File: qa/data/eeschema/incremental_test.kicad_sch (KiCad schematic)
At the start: 2 parts

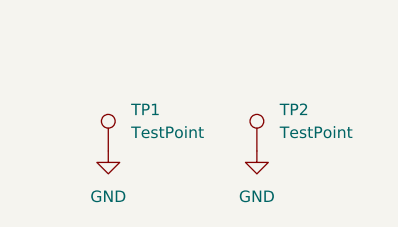
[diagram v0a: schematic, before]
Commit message: feat: update kicad to 9.0.0+dfsg-1
Signed-off-by: lhdjply <lhdjply@126.com>
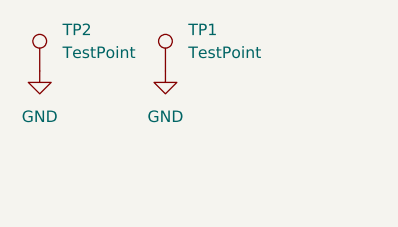
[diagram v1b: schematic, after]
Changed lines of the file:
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@@
 (kicad_sch
-	(version 20231120)
+	(version 20240101)
 	(generator "eeschema")
-	(generator_version "8.0")
+	(generator_version "8.99")
 	(paper "A4")
 	(symbol
+		(lib_id "power:GND")
+		(at 74.93 80.01 0)
+		(unit 1)
+		(exclude_from_sim no)
+		(in_bom yes)
+		(on_board yes)
+		(dnp no)
+		(fields_autoplaced yes)
+		(property "Reference" "#PWR03"
+			(at 74.93 86.36 0)
+			(effects
+				(font
+					(size 1.27 1.27)
+				)
+				(hide yes)
+			)
+		)
+		(property "Value" "GND"
+			(at 74.93 85.09 0)
+			(effects
+				(font
+					(size 1.27 1.27)
+				)
+			)
+		)
+		(property "Footprint" ""
+			(at 74.93 80.01 0)
+			(effects
+				(font
+					(size 1.27 1.27)
+				)
+				(hide yes)
+			)
+		)
+		(property "Datasheet" ""
+			(at 74.93 80.01 0)
+			(effects
+				(font
+					(size 1.27 1.27)
+				)
+				(hide yes)
+			)
+		)
+		(property "Description" "Power symbol creates a global label with name \"GND\" , ground"
+			(at 74.93 80.01 0)
+			(effects
+				(font
+					(size 1.27 1.27)
+				)
+				(hide yes)
+			)
+		)
+		(pin "1"
+		)
+		(instances
+			(project "incremental_test"
+				(path "/9c07925a-2c60-43f0-9bac-88be11f9747d"
+					(reference "#PWR03")
+					(unit 1)
+				)
+			)
+		)
+	)
+	(symbol
 		(lib_id "Connector:TestPoint")
-		(at 82.55 88.9 0)
+		(at 74.93 80.01 0)
+		(unit 1)
+		(exclude_from_sim no)
+		(in_bom yes)
+		(on_board yes)
+		(dnp no)
+		(fields_autoplaced yes)
+		(property "Reference" "TP2"
+			(at 77.47 75.4379 0)
+			(effects
+				(font
+					(size 1.27 1.27)
+				)
+				(justify left)
+			)
+		)
+		(property "Value" "TestPoint"
+			(at 77.47 77.9779 0)
+			(effects
+				(font
+					(size 1.27 1.27)
+				)
+				(justify left)
+			)
+		)
+		(property "Footprint" ""
+			(at 80.01 80.01 0)
+			(effects
+				(font
+					(size 1.27 1.27)
+				)
+				(hide yes)
+			)
+		)
+		(property "Datasheet" "~"
+			(at 80.01 80.01 0)
+			(effects
+				(font
+					(size 1.27 1.27)
+				)
+				(hide yes)
+			)
+		)
+		(property "Description" "test point"
+			(at 74.93 80.01 0)
+			(effects
+				(font
+					(size 1.27 1.27)
+				)
+				(hide yes)
+			)
+		)
+		(pin "1"
+		)
+		(instances
+			(project "incremental_test"
+				(path "/9c07925a-2c60-43f0-9bac-88be11f9747d"
+					(reference "TP2")
+					(unit 1)
+				)
+			)
+		)
+	)
+	(symbol
+		(lib_id "Connector:TestPoint")
+		(at 88.9 80.01 0)
 		(unit 1)
 		(exclude_from_sim no)
@@
 		(fields_autoplaced yes)
 		(property "Reference" "TP1"
-			(at 85.09 84.328 0)
+			(at 91.44 75.4379 0)
 			(effects
 				(font
@@
 		)
 		(property "Value" "TestPoint"
-			(at 85.09 86.868 0)
-			(effects
-				(font
-					(size 1.27 1.27)
-				)
-				(justify left)
-			)
-		)
-		(property "Footprint" ""
-			(at 87.63 88.9 0)
+			(at 91.44 77.9779 0)
+			(effects
+				(font
+					(size 1.27 1.27)
+				)
+				(justify left)
+			)
+		)
+		(property "Footprint" ""
+			(at 93.98 80.01 0)
 			(effects
 				(font
@@
 		)
 		(property "Datasheet" "~"
-			(at 87.63 88.9 0)
+			(at 93.98 80.01 0)
 			(effects
 				(font
@@
 		)
 		(property "Description" "test point"
-			(at 82.55 88.9 0)
-			(effects
-				(font
-					(size 1.27 1.27)
-				)
-				(hide yes)
-			)
-		)
-		(pin "1"
-		)
-		(instances
-			(project ""
-				(path "/5e4124ac-877c-4d6f-a16b-822110ac68a1"
+			(at 88.9 80.01 0)
+			(effects
+				(font
+					(size 1.27 1.27)
+				)
+				(hide yes)
+			)
+		)
+		(pin "1"
+		)
+		(instances
+			(project "incremental_test"
+				(path "/9c07925a-2c60-43f0-9bac-88be11f9747d"
 					(reference "TP1")
 					(unit 1)
@@
 	(symbol
 		(lib_id "power:GND")
-		(at 82.55 88.9 0)
+		(at 88.9 80.01 0)
 		(unit 1)
 		(exclude_from_sim no)
@@
 		(fields_autoplaced yes)
 		(property "Reference" "#PWR01"
-			(at 82.55 95.25 0)
+			(at 88.9 86.36 0)
 			(effects
 				(font
@@
 		)
 		(property "Value" "GND"
-			(at 82.55 93.98 0)
-			(effects
-				(font
-					(size 1.27 1.27)
-				)
-			)
-		)
-		(property "Footprint" ""
-			(at 82.55 88.9 0)
+			(at 88.9 85.09 0)
+			(effects
+				(font
+					(size 1.27 1.27)
+				)
+			)
+		)
+		(property "Footprint" ""
+			(at 88.9 80.01 0)
 			(effects
 				(font
@@
 		)
 		(property "Datasheet" ""
-			(at 82.55 88.9 0)
+			(at 88.9 80.01 0)
 			(effects
 				(font
@@
 		)
 		(property "Description" "Power symbol creates a global label with name \"GND\" , ground"
-			(at 82.55 88.9 0)
-			(effects
-				(font
-					(size 1.27 1.27)
-				)
-				(hide yes)
-			)
-		)
-		(pin "1"
-		)
-		(instances
-			(project ""
-				(path "/5e4124ac-877c-4d6f-a16b-822110ac68a1"
+			(at 88.9 80.01 0)
+			(effects
+				(font
+					(size 1.27 1.27)
+				)
+				(hide yes)
+			)
+		)
+		(pin "1"
+		)
+		(instances
+			(project "incremental_test"
+				(path "/9c07925a-2c60-43f0-9bac-88be11f9747d"
 					(reference "#PWR01")
 					(unit 1)
 				)
-			)
-		)
-	)
-	(symbol
-		(lib_id "Connector:TestPoint")
-		(at 99.06 88.9 0)
-		(unit 1)
-		(exclude_from_sim no)
-		(in_bom yes)
-		(on_board yes)
-		(dnp no)
-		(fields_autoplaced yes)
-		(property "Reference" "TP2"
-			(at 101.6 84.328 0)
-			(effects
-				(font
-					(size 1.27 1.27)
-				)
-				(justify left)
-			)
-		)
-		(property "Value" "TestPoint"
-			(at 101.6 86.868 0)
-			(effects
-				(font
-					(size 1.27 1.27)
-				)
-				(justify left)
-			)
-		)
-		(property "Footprint" ""
-			(at 104.14 88.9 0)
-			(effects
-				(font
-					(size 1.27 1.27)
-				)
-				(hide yes)
-			)
-		)
-		(property "Datasheet" "~"
-			(at 104.14 88.9 0)
-			(effects
-				(font
-					(size 1.27 1.27)
-				)
-				(hide yes)
-			)
-		)
-		(property "Description" "test point"
-			(at 99.06 88.9 0)
-			(effects
-				(font
-					(size 1.27 1.27)
-				)
-				(hide yes)
-			)
-		)
-		(pin "1"
-		)
-		(instances
-			(project ""
-				(path "/5e4124ac-877c-4d6f-a16b-822110ac68a1"
-					(reference "TP2")
-					(unit 1)
-				)
-			)
-		)
-	)
-	(symbol
-		(lib_id "power:GND")
-		(at 99.06 88.9 0)
-		(unit 1)
-		(exclude_from_sim no)
-		(in_bom yes)
-		(on_board yes)
-		(dnp no)
-		(fields_autoplaced yes)
-		(property "Reference" "#PWR02"
-			(at 99.06 95.25 0)
-			(effects
-				(font
-					(size 1.27 1.27)
-				)
-				(hide yes)
-			)
-		)
-		(property "Value" "GND"
-			(at 99.06 93.98 0)
-			(effects
-				(font
-					(size 1.27 1.27)
-				)
-			)
-		)
-		(property "Footprint" ""
-			(at 99.06 88.9 0)
-			(effects
-				(font
-					(size 1.27 1.27)
-				)
-				(hide yes)
-			)
-		)
-		(property "Datasheet" ""
-			(at 99.06 88.9 0)
-			(effects
-				(font
-					(size 1.27 1.27)
-				)
-				(hide yes)
-			)
-		)
-		(property "Description" "Power symbol creates a global label with name \"GND\" , ground"
-			(at 99.06 88.9 0)
-			(effects
-				(font
-					(size 1.27 1.27)
-				)
-				(hide yes)
-			)
-		)
-		(pin "1"
-		)
-		(instances
-			(project ""
-				(path "/5e4124ac-877c-4d6f-a16b-822110ac68a1"
-					(reference "#PWR02")
-					(unit 1)
-				)
